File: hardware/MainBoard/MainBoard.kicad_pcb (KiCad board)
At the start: 2 copper layers, 38.1 x 73.8 mm, 49 parts, among them J1 Conn_01x08_Socket, J2 Conn_01x08_Socket, J3 Conn_01x08_Socket, J4 Micro_SD_Card_Det2, J5 USB_C_Receptacle_USB2.0_16P, J8 En_A, Q1 MMBT2222A, U2 AMS1117-3.3, U3 AMS1117-5.0

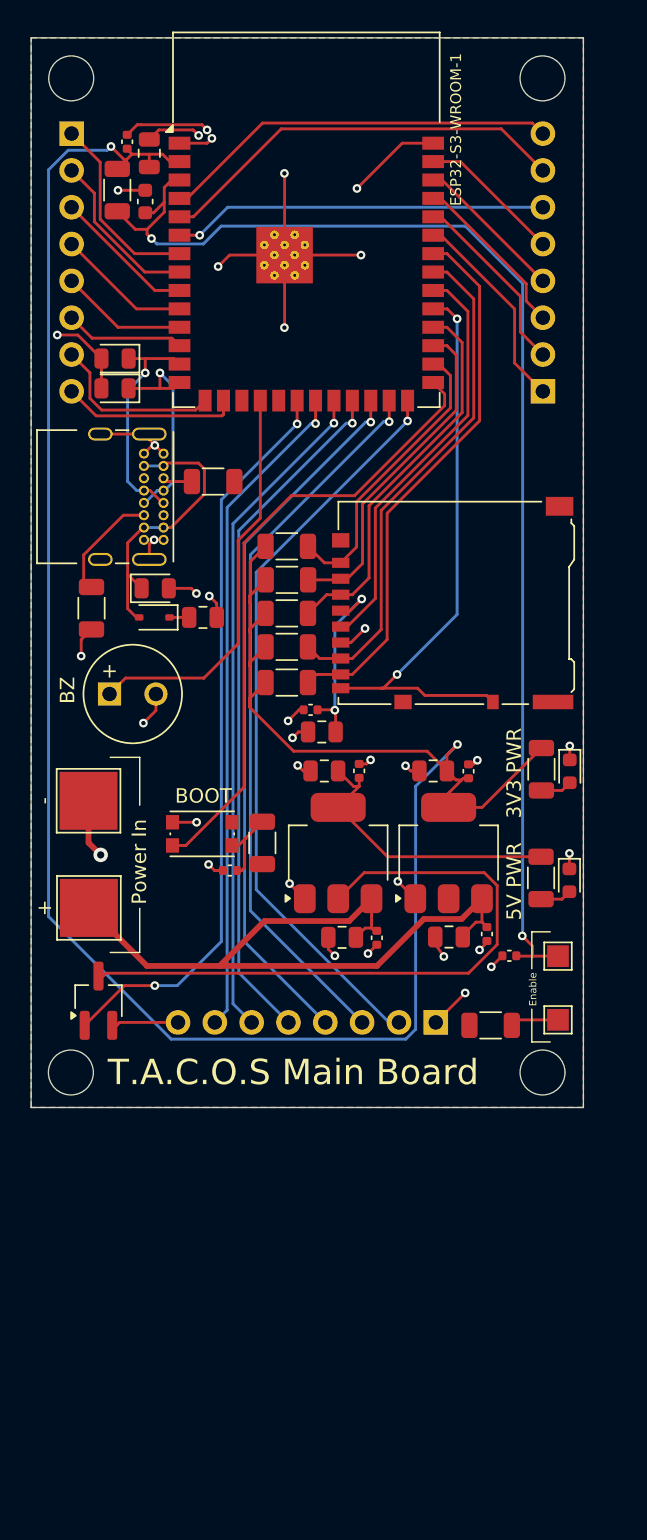
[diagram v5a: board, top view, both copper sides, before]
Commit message: added power from usb to main board
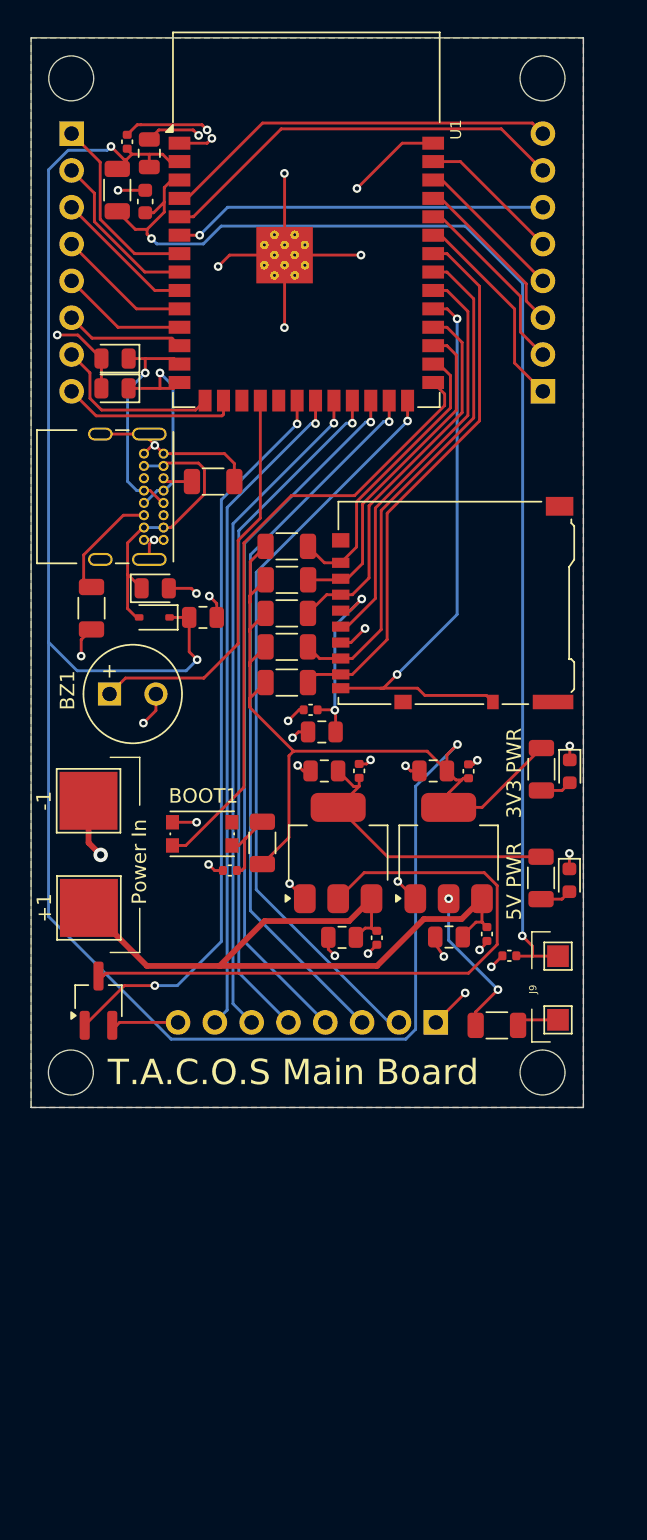
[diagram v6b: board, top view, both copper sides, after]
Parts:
- moved R5 0.43 mm to (82.9, 118.9)
- renumbered + to +1, - to -1, BOOT to BOOT1, BZ to BZ1, Enable to J9, ESP32-S3-WROOM-1 to U1
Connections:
- C1 pad 1: VCC_5V -> ESP_3V3
- D1 pad 1: VCC_5V -> ESP_3V3
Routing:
- net ESP_3V3: track 176.0 -> 211.4 mm, vias 4 -> 7
- net LIPO GND: track 93.7 -> 100.1 mm
- net VCC_5V: track 65.8 -> 64.5 mm
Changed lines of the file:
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@@
 			(layers "F.Cu" "F.Mask" "F.Paste")
 			(roundrect_rratio 0.25)
-			(net 24 "VCC_5V")
+			(net 25 "ESP_3V3")
 			(pintype "passive")
 		)
@@
 		(descr "CK components KMR2 tactile switch http://www.ckswitches.com/media/1479/kmr2.pdf")
 		(tags "tactile switch kmr2")
-		(property "Reference" "BOOT"
+		(property "Reference" "BOOT1"
 			(at 0.0836 -2.6143 180)
 			(layer "F.SilkS")
@@
 		(descr "SMD rectangular pad as test Point, square 1.5mm side length")
 		(tags "test point SMD pad rectangle square")
-		(property "Reference" "Enable"
+		(property "Reference" "J9"
 			(at 1.7272 -2.286 90)
 			(layer "F.SilkS")
@@
 		(descr "SMD rectangular pad as test Point, square 4.0mm side length")
 		(tags "test point SMD pad rectangle square")
-		(property "Reference" "-"
+		(property "Reference" "-1"
 			(at 0 -3.0734 90)
 			(layer "F.SilkS")
@@
 		(descr "SMD rectangular pad as test Point, square 4.0mm side length")
 		(tags "test point SMD pad rectangle square")
-		(property "Reference" "+"
+		(property "Reference" "+1"
 			(at 0 -3.0734 90)
 			(layer "F.SilkS")
@@
 	(footprint "Resistor_SMD:R_1206_3216Metric"
 		(layer "F.Cu")
-		(at 82.4992 118.9228)
+		(at 82.931 118.9228)
 		(descr "Resistor SMD 1206 (3216 Metric), square (rectangular) end terminal, IPC-7351 nominal, (Body size source: IPC-SM-782 page 72, https://www.pcb-3d.com/wordpress/wp-content/uploads/ipc-sm-782a_amendment_1_and_2.pdf), generated with kicad-footprint-generator")
 		(tags "resistor")
@@
 		(descr "Buzzer, Elektromagnetic Beeper, Summer,")
 		(tags "Kingstate KCG0601 ")
-		(property "Reference" "BZ"
+		(property "Reference" "BZ1"
 			(at -2.896 -0.254 90)
 			(layer "F.SilkS")
@@
 			(layers "F.Cu" "F.Mask" "F.Paste")
 			(roundrect_rratio 0.25)
-			(net 24 "VCC_5V")
+			(net 25 "ESP_3V3")
 			(pinfunction "K")
 			(pintype "passive")
@@
 		(descr "2.4 GHz Wi-Fi and Bluetooth module  https://www.espressif.com/sites/default/files/documentation/esp32-s3-wroom-1_wroom-1u_datasheet_en.pdf")
 		(tags "2.4 GHz Wi-Fi and Bluetooth module")
-		(property "Reference" "ESP32-S3-WROOM-1"
+		(property "Reference" "U1"
 			(at 10.3248 -6.1998 90)
 			(unlocked yes)
@@
 	)
 	(segment
-		(start 61.7055 90.7796)
-		(end 60.3527 90.7796)
-		(width 0.2)
-		(layer "F.Cu")
-		(net 24)
-	)
-	(segment
 		(start 73.045 102.4378)
 		(end 73.4314 102.4378)
@@
 	)
 	(segment
+		(start 68.5886 100.326857)
+		(end 68.907057 100.0084)
+		(width 0.2)
+		(layer "F.Cu")
+		(net 25)
+	)
+	(segment
 		(start 57.3893 59.1927)
 		(end 57.2115 59.1927)
@@
 	)
 	(segment
+		(start 61.7055 90.7796)
+		(end 61.7055 93.1507)
+		(width 0.2)
+		(layer "F.Cu")
+		(net 25)
+	)
+	(segment
 		(start 66.9758 95.2754)
 		(end 65.8876 96.3636)
@@
 	)
 	(segment
+		(start 81.4685 117.9977)
+		(end 83.0072 116.459)
+		(width 0.2)
+		(layer "F.Cu")
+		(net 25)
+	)
+	(segment
 		(start 65.8876 96.988943)
 		(end 68.907057 100.0084)
@@
 	)
 	(segment
+		(start 66.7512 107.7976)
+		(end 68.5886 105.9602)
+		(width 0.2)
+		(layer "F.Cu")
+		(net 25)
+	)
+	(segment
 		(start 65.8876 91.7448)
 		(end 65.8876 94.107)
@@
 	)
 	(segment
+		(start 68.5886 105.9602)
+		(end 68.5886 100.326857)
+		(width 0.2)
+		(layer "F.Cu")
+		(net 25)
+	)
+	(segment
 		(start 81.9114 103.8856)
 		(end 86.0044 99.7926)
@@
 	)
 	(segment
+		(start 81.4685 118.9228)
+		(end 81.4685 117.9977)
+		(width 0.2)
+		(layer "F.Cu")
+		(net 25)
+	)
+	(segment
 		(start 72.8048 90.314)
 		(end 73.6092 89.5096)
@@
 	)
 	(segment
+		(start 61.7055 93.1507)
+		(end 62.2554 93.7006)
+		(width 0.2)
+		(layer "F.Cu")
+		(net 25)
+	)
+	(segment
 		(start 68.907057 100.0084)
 		(end 78.1238 100.0084)
@@
 	)
 	(segment
+		(start 79.6036 110.1856)
+		(end 79.6036 110.109)
+		(width 0.2)
+		(layer "F.Cu")
+		(net 25)
+	)
+	(segment
 		(start 57.4294 58.5002)
 		(end 57.7556 58.8264)
@@
 	)
 	(segment
+		(start 61.7055 90.7796)
+		(end 60.3527 90.7796)
+		(width 0.2)
+		(layer "F.Cu")
+		(net 25)
+	)
+	(segment
 		(start 57.2115 59.1927)
 		(end 56.3118 58.293)
@@
 	)
 	(via
+		(at 83.0072 116.459)
+		(size 0.6)
+		(drill 0.3)
+		(layers "F.Cu" "B.Cu")
+		(net 25)
+	)
+	(via
+		(at 62.2554 93.7006)
+		(size 0.6)
+		(drill 0.3)
+		(layers "F.Cu" "B.Cu")
+		(net 25)
+	)
+	(via
+		(at 79.6036 110.1856)
+		(size 0.6)
+		(drill 0.3)
+		(layers "F.Cu" "B.Cu")
+		(net 25)
+	)
+	(via
 		(at 73.6092 89.5096)
 		(size 0.6)
@@
 	)
 	(segment
-		(start 52.0024 111.41516)
+		(start 52.0024 92.4814)
 		(end 52.0024 59.90784)
 		(width 0.2)
@@
 	)
 	(segment
+		(start 61.4934 94.4626)
+		(end 53.9836 94.4626)
+		(width 0.2)
+		(layer "B.Cu")
+		(net 25)
+	)
+	(segment
 		(start 73.6092 89.5096)
 		(end 71.755 91.3638)
@@
 	)
 	(segment
+		(start 79.6036 113.0554)
+		(end 79.6036 110.1856)
+		(width 0.2)
+		(layer "B.Cu")
+		(net 25)
+	)
+	(segment
 		(start 76.65136 119.8706)
 		(end 60.45784 119.8706)
@@
 	)
 	(segment
+		(start 52.0024 111.41516)
+		(end 52.0024 92.4814)
+		(width 0.2)
+		(layer "B.Cu")
+		(net 25)
+	)
+	(segment
 		(start 80.2132 99.5426)
 		(end 77.3256 102.4302)
@@
 	)
 	(segment
+		(start 62.2554 93.7006)
+		(end 61.4934 94.4626)
+		(width 0.2)
+		(layer "B.Cu")
+		(net 25)
+	)
+	(segment
 		(start 52.0024 59.90784)
 		(end 53.35524 58.555)
@@
 	)
 	(segment
+		(start 53.9836 94.4626)
+		(end 52.0024 92.4814)
+		(width 0.2)
+		(layer "B.Cu")
+		(net 25)
+	)
+	(segment
+		(start 83.0072 116.459)
+		(end 79.6036 113.0554)
+		(width 0.2)
+		(layer "B.Cu")
+		(net 25)
+	)
+	(segment
 		(start 60.5536 106.5129)
 		(end 61.469043 106.5129)
@@
 	)
 	(segment
+		(start 64.8208 80.1624)
+		(end 64.1388 79.4804)
+		(width 0.2)
+		(layer "F.Cu")
+		(net 42)
+	)
+	(segment
 		(start 54.7624 103.4288)
 		(end 54.7624 106.3244)
@@
 	)
 	(segment
+		(start 64.1388 79.4804)
+		(end 59.9352 79.4804)
+		(width 0.2)
+		(layer "F.Cu")
+		(net 42)
+	)
+	(segment
 		(start 59.3662 78.9114)
 		(end 59.9352 79.4804)
@@
 	)
 	(segment
+		(start 64.8208 81.407)
+		(end 64.8208 80.1624)
+		(width 0.2)
+		(layer "F.Cu")
+		(net 42)
+	)
+	(segment
 		(start 73.9394 100.8888)
 		(end 74.2188 100.6094)
@@
 	(segment
 		(start 87.1474 118.5418)
-		(end 84.3427 118.5418)
+		(end 84.7745 118.5418)
 		(width 0.2)
 		(layer "F.Cu")
@@
 	)
 	(segment
-		(start 84.3427 118.5418)
-		(end 83.9617 118.9228)
+		(start 84.7745 118.5418)
+		(end 84.3935 118.9228)
 		(width 0.2)
 		(layer "F.Cu")

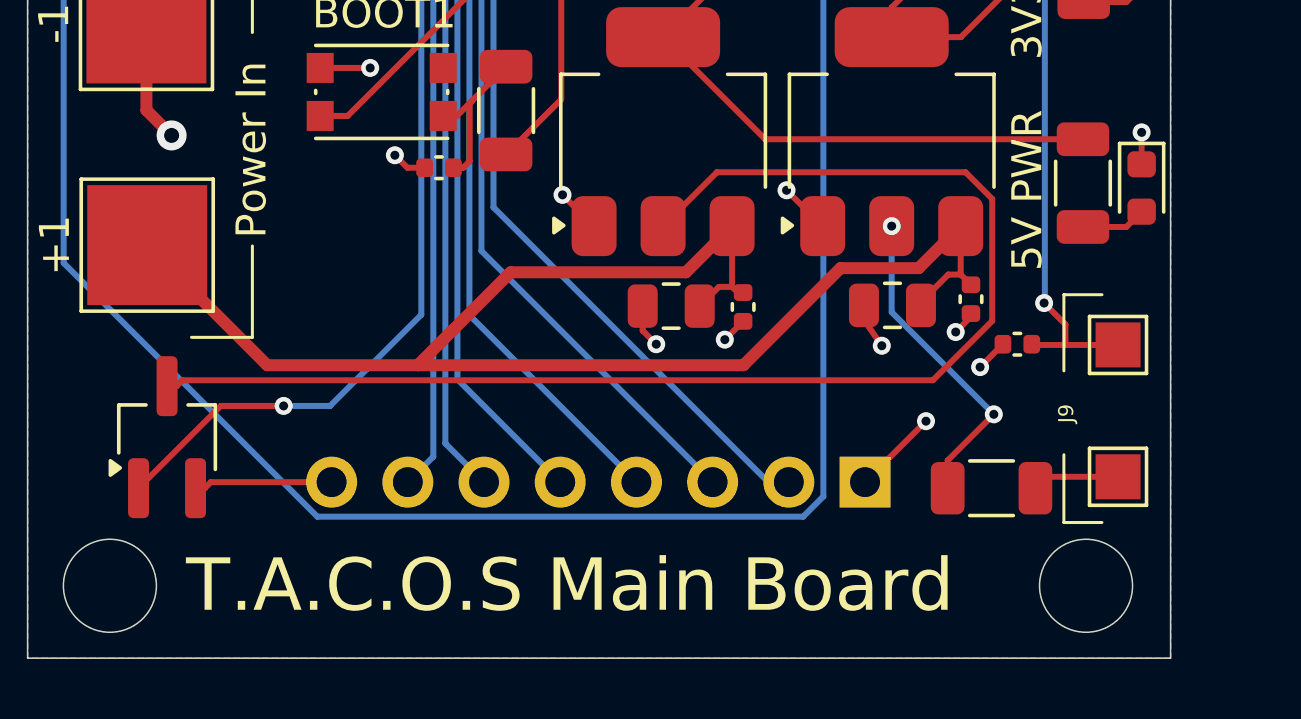
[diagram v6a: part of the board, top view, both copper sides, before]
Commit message: tacos logo and font change
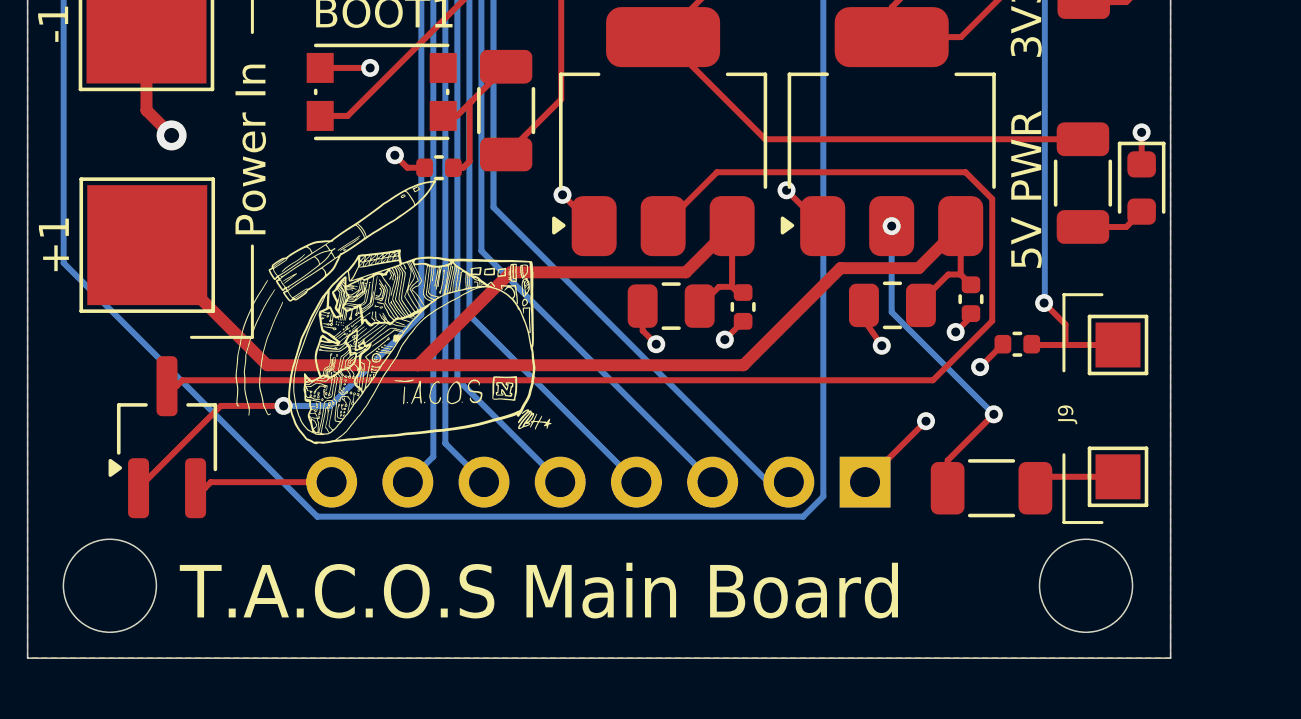
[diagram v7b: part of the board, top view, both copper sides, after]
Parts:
- added G***: LOGO, lib:tacos_logo, F.Cu at (66.4, 103.8)
